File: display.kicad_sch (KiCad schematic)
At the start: 17 parts

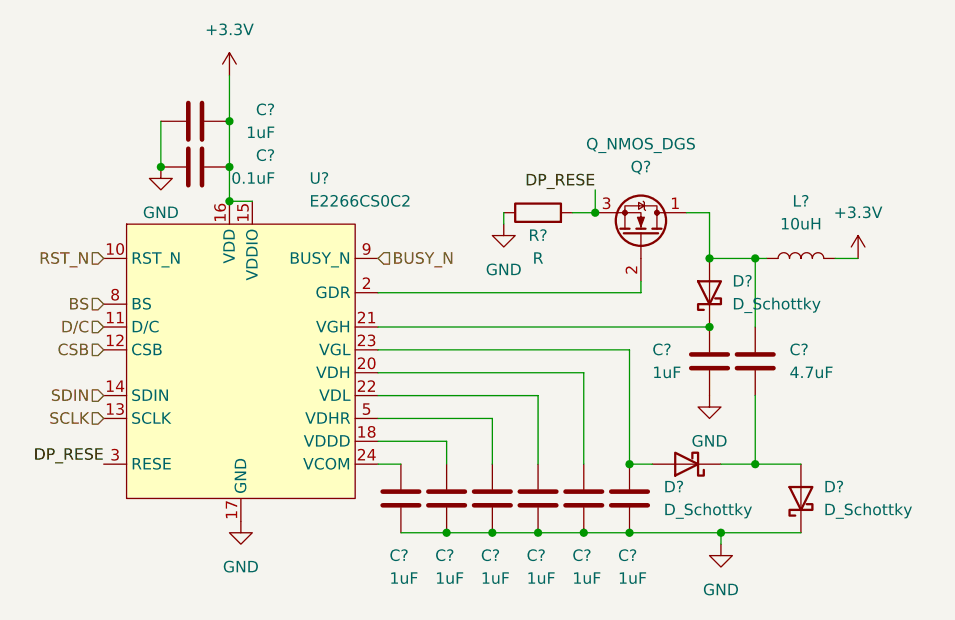
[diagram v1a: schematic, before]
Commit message: added audio ref schematic, added bat to 5V, added shift register, connected devices with other periferals
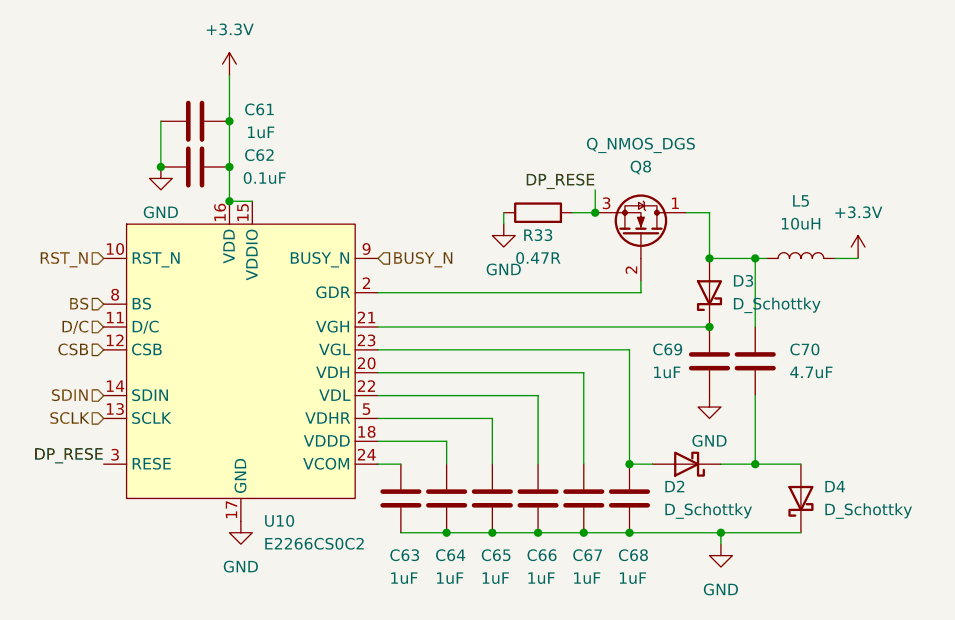
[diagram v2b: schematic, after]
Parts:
- R33: renamed from R?; value R -> 0.47R
- gave numbers to parts that had none: 16
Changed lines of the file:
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@@
   (symbol (lib_id "Device:C") (at 182.88 107.95 180) (unit 1)
     (in_bom yes) (on_board yes)
-    (property "Reference" "C?" (id 0) (at 181.61 114.3 0)
+    (property "Reference" "C67" (id 0) (at 181.61 114.3 0)
       (effects (font (size 1.27 1.27)) (justify right))
     )
@@
   (symbol (lib_id "Device:Q_NMOS_DGS") (at 189.23 78.74 270) (mirror x) (unit 1)
     (in_bom yes) (on_board yes)
-    (property "Reference" "Q?" (id 0) (at 189.23 71.12 90))
+    (property "Reference" "Q8" (id 0) (at 189.23 71.12 90))
     (property "Value" "Q_NMOS_DGS" (id 1) (at 189.23 68.58 90))
     (property "Footprint" "" (id 2) (at 191.77 73.66 0)
@@
   (symbol (lib_id "Device:D_Schottky") (at 196.85 85.09 90) (unit 1)
     (in_bom yes) (on_board yes)
-    (property "Reference" "D?" (id 0) (at 199.39 83.82 90)
+    (property "Reference" "D3" (id 0) (at 199.39 83.82 90)
       (effects (font (size 1.27 1.27)) (justify right))
     )
@@
   (symbol (lib_id "Device:C") (at 187.96 107.95 180) (unit 1)
     (in_bom yes) (on_board yes)
-    (property "Reference" "C?" (id 0) (at 186.69 114.3 0)
+    (property "Reference" "C68" (id 0) (at 186.69 114.3 0)
       (effects (font (size 1.27 1.27)) (justify right))
     )
@@
   (symbol (lib_id "Device:C") (at 162.56 107.95 180) (unit 1)
     (in_bom yes) (on_board yes)
-    (property "Reference" "C?" (id 0) (at 161.29 114.3 0)
+    (property "Reference" "C63" (id 0) (at 161.29 114.3 0)
       (effects (font (size 1.27 1.27)) (justify right))
     )
@@
   (symbol (lib_id "Device:C") (at 167.64 107.95 180) (unit 1)
     (in_bom yes) (on_board yes)
-    (property "Reference" "C?" (id 0) (at 166.37 114.3 0)
+    (property "Reference" "C64" (id 0) (at 166.37 114.3 0)
       (effects (font (size 1.27 1.27)) (justify right))
     )
@@
   (symbol (lib_id "Device:C") (at 139.7 71.12 270) (unit 1)
     (in_bom yes) (on_board yes)
-    (property "Reference" "C?" (id 0) (at 148.59 69.85 90)
-      (effects (font (size 1.27 1.27)) (justify right))
-    )
-    (property "Value" "0.1uF" (id 1) (at 148.59 72.39 90)
+    (property "Reference" "C62" (id 0) (at 148.59 69.85 90)
+      (effects (font (size 1.27 1.27)) (justify right))
+    )
+    (property "Value" "0.1uF" (id 1) (at 149.86 72.39 90)
       (effects (font (size 1.27 1.27)) (justify right))
     )
@@
   (symbol (lib_id "Device:D_Schottky") (at 207.01 107.95 90) (unit 1)
     (in_bom yes) (on_board yes)
-    (property "Reference" "D?" (id 0) (at 209.55 106.68 90)
+    (property "Reference" "D4" (id 0) (at 209.55 106.68 90)
       (effects (font (size 1.27 1.27)) (justify right))
     )
@@
   (symbol (lib_id "Device:C") (at 139.7 66.04 270) (unit 1)
     (in_bom yes) (on_board yes)
-    (property "Reference" "C?" (id 0) (at 148.59 64.77 90)
+    (property "Reference" "C61" (id 0) (at 148.59 64.77 90)
       (effects (font (size 1.27 1.27)) (justify right))
     )
@@
   (symbol (lib_id "Device:R") (at 177.8 76.2 90) (unit 1)
     (in_bom yes) (on_board yes)
-    (property "Reference" "R?" (id 0) (at 177.8 78.74 90))
-    (property "Value" "R" (id 1) (at 177.8 81.28 90))
+    (property "Reference" "R33" (id 0) (at 177.8 78.74 90))
+    (property "Value" "0.47R" (id 1) (at 177.8 81.28 90))
     (property "Footprint" "" (id 2) (at 177.8 77.978 90)
       (effects (font (size 1.27 1.27)) hide)
@@
   (symbol (lib_id "Device:C") (at 177.8 107.95 180) (unit 1)
     (in_bom yes) (on_board yes)
-    (property "Reference" "C?" (id 0) (at 176.53 114.3 0)
+    (property "Reference" "C66" (id 0) (at 176.53 114.3 0)
       (effects (font (size 1.27 1.27)) (justify right))
     )
@@
   (symbol (lib_id "Device:D_Schottky") (at 194.31 104.14 180) (unit 1)
     (in_bom yes) (on_board yes)
-    (property "Reference" "D?" (id 0) (at 191.77 106.68 0)
+    (property "Reference" "D2" (id 0) (at 191.77 106.68 0)
       (effects (font (size 1.27 1.27)) (justify right))
     )
@@
   (symbol (lib_id "Device:C") (at 172.72 107.95 180) (unit 1)
     (in_bom yes) (on_board yes)
-    (property "Reference" "C?" (id 0) (at 171.45 114.3 0)
+    (property "Reference" "C65" (id 0) (at 171.45 114.3 0)
       (effects (font (size 1.27 1.27)) (justify right))
     )
@@
   (symbol (lib_id "Device:L") (at 207.01 81.28 90) (unit 1)
     (in_bom yes) (on_board yes) (fields_autoplaced)
-    (property "Reference" "L?" (id 0) (at 207.01 74.93 90))
+    (property "Reference" "L5" (id 0) (at 207.01 74.93 90))
     (property "Value" "10uH" (id 1) (at 207.01 77.47 90))
     (property "Footprint" "" (id 2) (at 207.01 81.28 0)
@@
   (symbol (lib_id "Device:C") (at 196.85 92.71 180) (unit 1)
     (in_bom yes) (on_board yes)
-    (property "Reference" "C?" (id 0) (at 190.5 91.44 0)
+    (property "Reference" "C69" (id 0) (at 190.5 91.44 0)
       (effects (font (size 1.27 1.27)) (justify right))
     )
@@
   (symbol (lib_id "Device:C") (at 201.93 92.71 180) (unit 1)
     (in_bom yes) (on_board yes)
-    (property "Reference" "C?" (id 0) (at 205.74 91.44 0)
+    (property "Reference" "C70" (id 0) (at 205.74 91.44 0)
       (effects (font (size 1.27 1.27)) (justify right))
     )
@@
   (symbol (lib_id "airsoft_controller:E2266CS0C2") (at 144.78 92.71 0) (unit 1)
     (in_bom yes) (on_board yes)
-    (property "Reference" "U?" (id 0) (at 152.4 72.39 0)
+    (property "Reference" "U10" (id 0) (at 147.32 110.49 0)
       (effects (font (size 1.27 1.27)) (justify left))
     )
-    (property "Value" "E2266CS0C2" (id 1) (at 152.4 74.93 0)
+    (property "Value" "E2266CS0C2" (id 1) (at 147.32 113.03 0)
       (effects (font (size 1.27 1.27)) (justify left))
     )

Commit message: added adcin2 config description, fixed some rule check errors
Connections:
- now unconnected: U10.1 (NC), U10.19 (NC), U10.4 (NC), U10.6 (NC), U10.7 (NC)

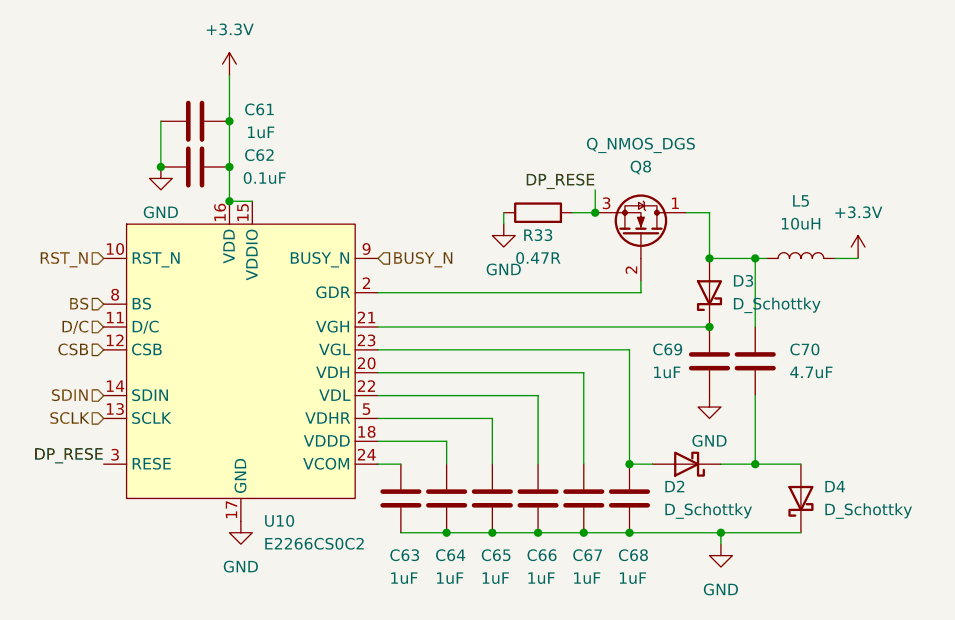
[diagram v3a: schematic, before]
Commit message: minor optimized pinassignement, added capacitors, added connectors
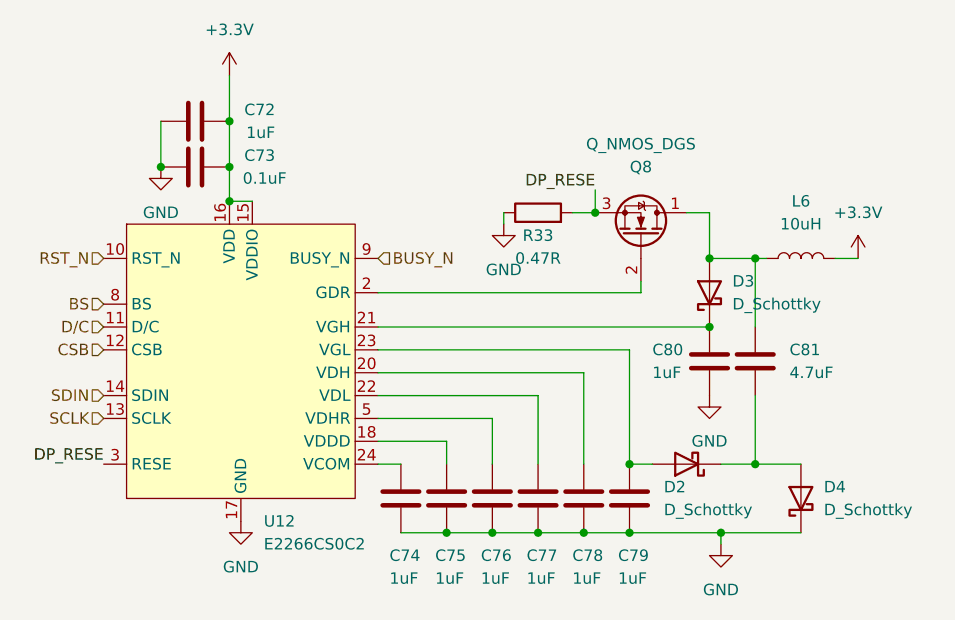
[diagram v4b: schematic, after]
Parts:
- renumbered C61 to C72, C62 to C73, C63 to C74, C64 to C75, C65 to C76, C66 to C77, C67 to C78, C68 to C79, C69 to C80, C70 to C81, L5 to L6, U10 to U12
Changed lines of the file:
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@@
   (symbol (lib_id "Device:C") (at 182.88 107.95 180) (unit 1)
     (in_bom yes) (on_board yes)
-    (property "Reference" "C67" (id 0) (at 181.61 114.3 0)
+    (property "Reference" "C78" (id 0) (at 181.61 114.3 0)
       (effects (font (size 1.27 1.27)) (justify right))
     )
@@
   (symbol (lib_id "power:GND") (at 196.85 96.52 0) (unit 1)
     (in_bom yes) (on_board yes) (fields_autoplaced)
-    (property "Reference" "#PWR0177" (id 0) (at 196.85 102.87 0)
+    (property "Reference" "#PWR095" (id 0) (at 196.85 102.87 0)
       (effects (font (size 1.27 1.27)) hide)
     )
@@
   (symbol (lib_id "power:GND") (at 135.89 71.12 0) (unit 1)
     (in_bom yes) (on_board yes) (fields_autoplaced)
-    (property "Reference" "#PWR0178" (id 0) (at 135.89 77.47 0)
+    (property "Reference" "#PWR091" (id 0) (at 135.89 77.47 0)
       (effects (font (size 1.27 1.27)) hide)
     )
@@
   (symbol (lib_id "power:GND") (at 144.78 110.49 0) (unit 1)
     (in_bom yes) (on_board yes) (fields_autoplaced)
-    (property "Reference" "#PWR0179" (id 0) (at 144.78 116.84 0)
+    (property "Reference" "#PWR093" (id 0) (at 144.78 116.84 0)
       (effects (font (size 1.27 1.27)) hide)
     )
@@
   (symbol (lib_id "Device:C") (at 187.96 107.95 180) (unit 1)
     (in_bom yes) (on_board yes)
-    (property "Reference" "C68" (id 0) (at 186.69 114.3 0)
+    (property "Reference" "C79" (id 0) (at 186.69 114.3 0)
       (effects (font (size 1.27 1.27)) (justify right))
     )
@@
   (symbol (lib_id "power:+3.3V") (at 143.51 60.96 0) (unit 1)
     (in_bom yes) (on_board yes) (fields_autoplaced)
-    (property "Reference" "#PWR0180" (id 0) (at 143.51 64.77 0)
+    (property "Reference" "#PWR092" (id 0) (at 143.51 64.77 0)
       (effects (font (size 1.27 1.27)) hide)
     )
@@
   (symbol (lib_id "Device:C") (at 162.56 107.95 180) (unit 1)
     (in_bom yes) (on_board yes)
-    (property "Reference" "C63" (id 0) (at 161.29 114.3 0)
+    (property "Reference" "C74" (id 0) (at 161.29 114.3 0)
       (effects (font (size 1.27 1.27)) (justify right))
     )
@@
   (symbol (lib_id "Device:C") (at 167.64 107.95 180) (unit 1)
     (in_bom yes) (on_board yes)
-    (property "Reference" "C64" (id 0) (at 166.37 114.3 0)
+    (property "Reference" "C75" (id 0) (at 166.37 114.3 0)
       (effects (font (size 1.27 1.27)) (justify right))
     )
@@
   (symbol (lib_id "Device:C") (at 139.7 71.12 270) (unit 1)
     (in_bom yes) (on_board yes)
-    (property "Reference" "C62" (id 0) (at 148.59 69.85 90)
+    (property "Reference" "C73" (id 0) (at 148.59 69.85 90)
       (effects (font (size 1.27 1.27)) (justify right))
     )
@@
   (symbol (lib_id "power:+3.3V") (at 213.36 81.28 0) (unit 1)
     (in_bom yes) (on_board yes) (fields_autoplaced)
-    (property "Reference" "#PWR0174" (id 0) (at 213.36 85.09 0)
+    (property "Reference" "#PWR097" (id 0) (at 213.36 85.09 0)
       (effects (font (size 1.27 1.27)) hide)
     )
@@
   (symbol (lib_id "power:GND") (at 173.99 77.47 0) (unit 1)
     (in_bom yes) (on_board yes) (fields_autoplaced)
-    (property "Reference" "#PWR0175" (id 0) (at 173.99 83.82 0)
+    (property "Reference" "#PWR094" (id 0) (at 173.99 83.82 0)
       (effects (font (size 1.27 1.27)) hide)
     )
@@
   (symbol (lib_id "Device:C") (at 139.7 66.04 270) (unit 1)
     (in_bom yes) (on_board yes)
-    (property "Reference" "C61" (id 0) (at 148.59 64.77 90)
+    (property "Reference" "C72" (id 0) (at 148.59 64.77 90)
       (effects (font (size 1.27 1.27)) (justify right))
     )
@@
   (symbol (lib_id "Device:C") (at 177.8 107.95 180) (unit 1)
     (in_bom yes) (on_board yes)
-    (property "Reference" "C66" (id 0) (at 176.53 114.3 0)
+    (property "Reference" "C77" (id 0) (at 176.53 114.3 0)
       (effects (font (size 1.27 1.27)) (justify right))
     )
@@
   (symbol (lib_id "Device:C") (at 172.72 107.95 180) (unit 1)
     (in_bom yes) (on_board yes)
-    (property "Reference" "C65" (id 0) (at 171.45 114.3 0)
+    (property "Reference" "C76" (id 0) (at 171.45 114.3 0)
       (effects (font (size 1.27 1.27)) (justify right))
     )
@@
   (symbol (lib_id "Device:L") (at 207.01 81.28 90) (unit 1)
     (in_bom yes) (on_board yes) (fields_autoplaced)
-    (property "Reference" "L5" (id 0) (at 207.01 74.93 90))
+    (property "Reference" "L6" (id 0) (at 207.01 74.93 90))
     (property "Value" "10uH" (id 1) (at 207.01 77.47 90))
     (property "Footprint" "" (id 2) (at 207.01 81.28 0)
@@
   (symbol (lib_id "power:GND") (at 198.12 113.03 0) (unit 1)
     (in_bom yes) (on_board yes) (fields_autoplaced)
-    (property "Reference" "#PWR0176" (id 0) (at 198.12 119.38 0)
+    (property "Reference" "#PWR096" (id 0) (at 198.12 119.38 0)
       (effects (font (size 1.27 1.27)) hide)
     )
@@
   (symbol (lib_id "Device:C") (at 196.85 92.71 180) (unit 1)
     (in_bom yes) (on_board yes)
-    (property "Reference" "C69" (id 0) (at 190.5 91.44 0)
+    (property "Reference" "C80" (id 0) (at 190.5 91.44 0)
       (effects (font (size 1.27 1.27)) (justify right))
     )
@@
   (symbol (lib_id "Device:C") (at 201.93 92.71 180) (unit 1)
     (in_bom yes) (on_board yes)
-    (property "Reference" "C70" (id 0) (at 205.74 91.44 0)
+    (property "Reference" "C81" (id 0) (at 205.74 91.44 0)
       (effects (font (size 1.27 1.27)) (justify right))
     )
@@
   (symbol (lib_id "airsoft_controller:E2266CS0C2") (at 144.78 92.71 0) (unit 1)
     (in_bom yes) (on_board yes)
-    (property "Reference" "U10" (id 0) (at 147.32 110.49 0)
+    (property "Reference" "U12" (id 0) (at 147.32 110.49 0)
       (effects (font (size 1.27 1.27)) (justify left))
     )
